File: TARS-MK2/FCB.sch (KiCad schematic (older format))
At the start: 30 parts, among them J101 505567-0681, J102 505567-0681, J103 505567-0681, J104 505567-0681, J105 505578-0671, J106 505578-0671, U101 LSM9DS1, U102 KX122-1711, U103 MS5611-01BA, U104 MPU-9250, U105 ublox_SAM-M8Q

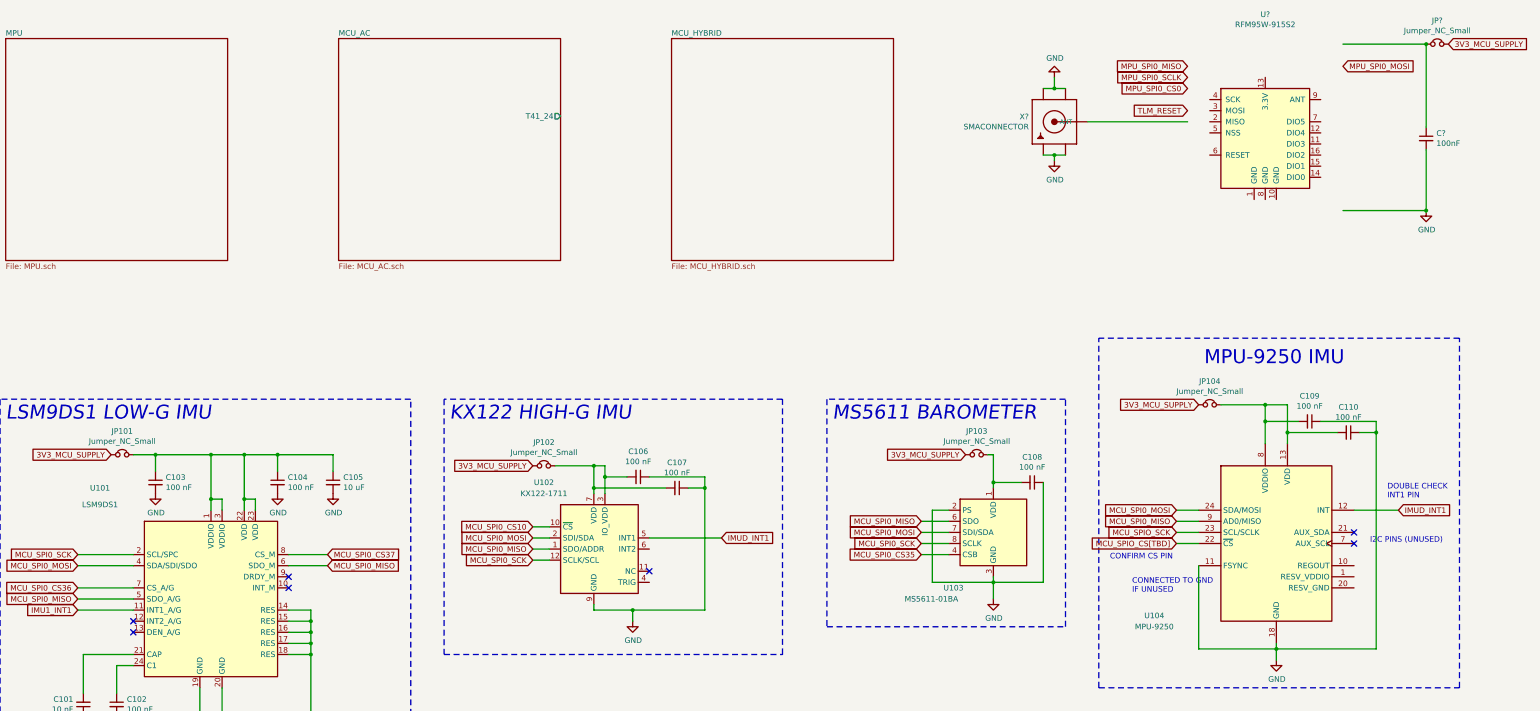
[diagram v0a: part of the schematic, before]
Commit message: Added MPU SYSBOOT config resistors
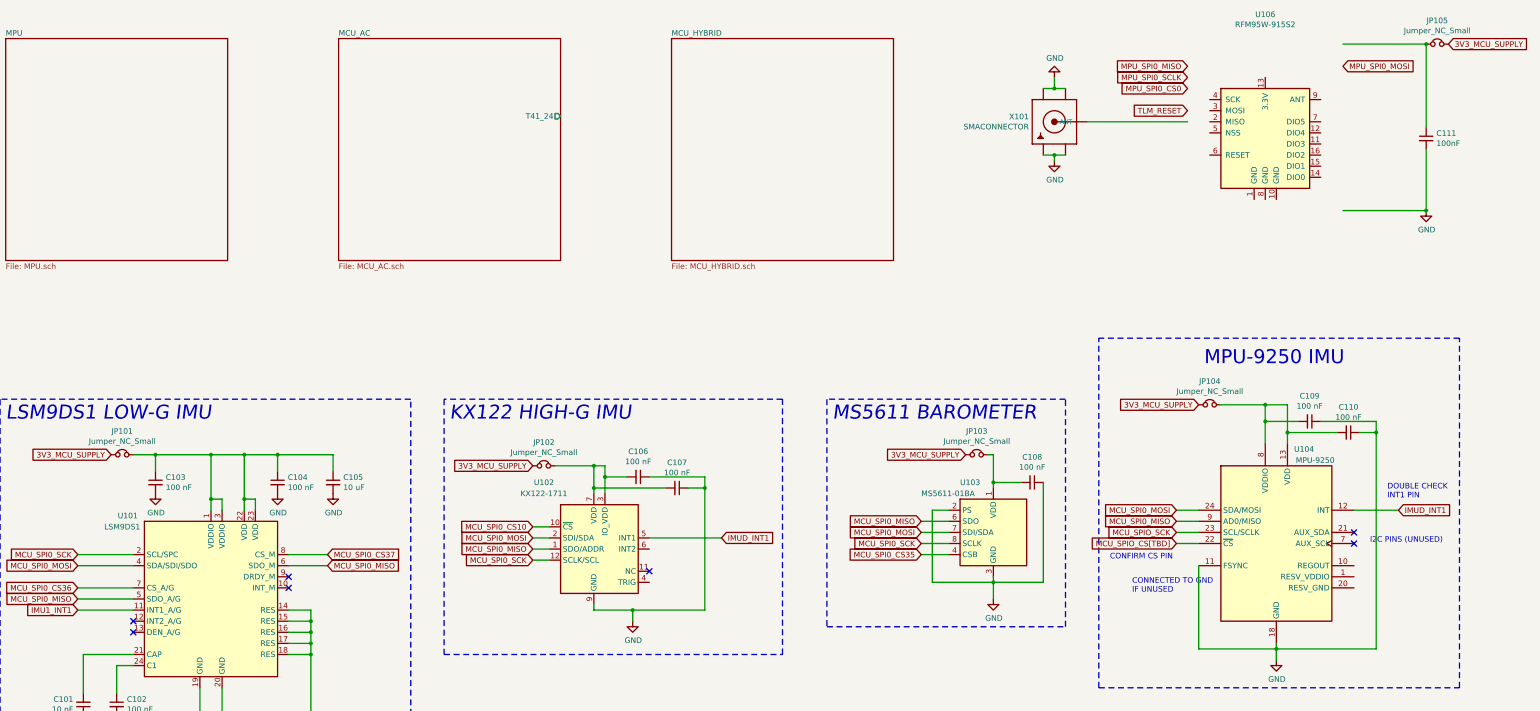
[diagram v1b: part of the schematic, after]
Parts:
- gave numbers to parts that had none: 4
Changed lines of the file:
@@
 F1 "MPU.sch" 50
-$EndSheet
-$Sheet
-S 7800 1500 2000 2000
-U 60021F93
-F0 "MCU_HYBRID" 50
-F1 "MCU_HYBRID.sch" 50
 $EndSheet
 Text Notes 11850 10500 0    67   Italic 0
@@
 U 1 1 602F3A3E
 P 10700 5950
-F 0 "U103" H 10250 5450 50  0000 L CNN
-F 1 "MS5611-01BA" H 9900 5350 50  0000 L CNN
+F 0 "U103" H 10400 6400 50  0000 L CNN
+F 1 "MS5611-01BA" H 10050 6300 50  0000 L CNN
 F 2 "Package_LGA:LGA-8_3x5mm_P1.25mm" H 10700 5950 50  0001 C CNN
 F 3 "https://www.te.com/commerce/DocumentDelivery/DDEController?Action=srchrtrv&DocNm=MS5611-01BA03&DocType=Data+Sheet&DocLang=English" H 10700 5950 50  0001 C CNN
@@
 Wire Wire Line
 	2450 6450 2950 6450
-Wire Wire Line
-	2450 6250 2950 6250
 Wire Wire Line
 	2450 6150 2950 6150
@@
 Text GLabel 2450 6450 0    50   Input ~ 0
 MCU_SPI0_CS36
-Text GLabel 2450 6250 0    50   Input ~ 0
-MCU_SPI0_MOSI
 Text GLabel 2450 6150 0    50   Input ~ 0
 MCU_SPI0_SCK
@@
 U 1 1 602BFCA3
 P 3650 6550
-F 0 "U101" H 2650 7550 50  0000 C CNN
-F 1 "LSM9DS1" H 2650 7400 50  0000 C CNN
+F 0 "U101" H 2900 7300 50  0000 C CNN
+F 1 "LSM9DS1" H 2850 7200 50  0000 C CNN
 F 2 "Package_LGA:LGA-24L_3x3.5mm_P0.43mm" H 5150 7300 50  0001 C CNN
 F 3 "http://www.st.com/content/ccc/resource/technical/document/datasheet/1e/3f/2a/d6/25/eb/48/46/DM00103319.pdf/files/DM00103319.pdf/jcr:content/translations/en.DM00103319.pdf" H 3650 6650 50  0001 C CNN
@@
 	0    -1   1    0
 $EndComp
-$Sheet
-S 4800 1500 2000 2000
-U 60021F5A
-F0 "MCU_AC" 50
-F1 "MCU_AC.sch" 50
-F2 "T41_24" O R 6800 2200 50
-$EndSheet
 Connection ~ 7100 5550
 Wire Wire Line
@@
 	13250 7100 13250 7000
 $Comp
-L power:GND #PWR?
+L power:GND #PWR0165
 U 1 1 606711D2
 P 13250 7100
-F 0 "#PWR?" H 13250 6850 50  0001 C CNN
+F 0 "#PWR0165" H 13250 6850 50  0001 C CNN
 F 1 "GND" H 13255 6927 50  0000 C CNN
 F 2 "" H 13250 7100 50  0001 C CNN
@@
 U 1 1 604AA87B
 P 13250 6050
-F 0 "U104" H 12150 5400 50  0000 C CNN
-F 1 "MPU-9250" H 12150 5300 50  0000 C CNN
+F 0 "U104" H 13500 6900 50  0000 C CNN
+F 1 "MPU-9250" H 13600 6800 50  0000 C CNN
 F 2 "Sensor_Motion:InvenSense_QFN-24_3x3mm_P0.4mm" H 13250 5050 50  0001 C CNN
 F 3 "https://store.invensense.com/datasheets/invensense/MPU9250REV1.0.pdf" H 13250 5900 50  0001 C CNN
@@
 MPU_SPI0_MOSI
 $Comp
-L RFM95W_915S2:RFM95W-915S2 U?
+L RFM95W_915S2:RFM95W-915S2 U106
 U 1 1 604CFE3B
 P 13150 2350
-F 0 "U?" H 13150 3417 50  0000 C CNN
+F 0 "U106" H 13150 3417 50  0000 C CNN
 F 1 "RFM95W-915S2" H 13150 3326 50  0000 C CNN
 F 2 "XCVR_RFM95W-915S2" H 13150 2350 50  0001 L BNN
@@
 	13850 1550 14600 1550
 $Comp
-L power:GND #PWR?
+L power:GND #PWR0166
 U 1 1 604E0CB3
 P 14600 3050
-F 0 "#PWR?" H 14600 2800 50  0001 C CNN
+F 0 "#PWR0166" H 14600 2800 50  0001 C CNN
 F 1 "GND" H 14605 2877 50  0000 C CNN
 F 2 "" H 14600 3050 50  0001 C CNN
@@
 $EndComp
 $Comp
-L D24V50F5:C_Small C?
+L D24V50F5:C_Small C111
 U 1 1 604E53FE
 P 14600 2400
-F 0 "C?" H 14692 2446 50  0000 L CNN
+F 0 "C111" H 14692 2446 50  0000 L CNN
 F 1 "100nF" H 14692 2355 50  0000 L CNN
 F 2 "" H 14600 2400 50  0001 C CNN
@@
 $EndComp
 $Comp
-L D24V50F5:Jumper_NC_Small JP?
+L D24V50F5:Jumper_NC_Small JP105
 U 1 1 604E6165
 P 14700 1550
-F 0 "JP?" H 14700 1762 50  0000 C CNN
+F 0 "JP105" H 14700 1762 50  0000 C CNN
 F 1 "Jumper_NC_Small" H 14700 1671 50  0000 C CNN
 F 2 "" H 14700 1550 50  0001 C CNN
@@
 $EndComp
 $Comp
-L SMACONNECTOR:SMACONNECTOR X?
+L SMACONNECTOR:SMACONNECTOR X101
 U 1 1 604E7810
 P 11250 2250
-F 0 "X?" H 11480 2204 50  0000 L CNN
+F 0 "X101" H 11480 2204 50  0000 L CNN
 F 1 "SMACONNECTOR" H 11480 2295 50  0000 L CNN
 F 2 "" H 11250 2250 50  0001 C CNN
@@
 	11150 2550 11250 2550
 $Comp
-L power:GND #PWR?
+L power:GND #PWR0167
 U 1 1 604F94E4
 P 11250 2600
-F 0 "#PWR?" H 11250 2350 50  0001 C CNN
+F 0 "#PWR0167" H 11250 2350 50  0001 C CNN
 F 1 "GND" H 11255 2427 50  0000 C CNN
 F 2 "" H 11250 2600 50  0001 C CNN
@@
 	11250 2550 11350 2550
 $Comp
-L power:GND #PWR?
+L power:GND #PWR0168
 U 1 1 604FE003
 P 11250 1850
-F 0 "#PWR?" H 11250 1600 50  0001 C CNN
+F 0 "#PWR0168" H 11250 1600 50  0001 C CNN
 F 1 "GND" H 11255 1677 50  0000 C CNN
 F 2 "" H 11250 1850 50  0001 C CNN
@@
 Wire Wire Line
 	12450 2250 11550 2250
+$Sheet
+S 7800 1500 2000 2000
+U 60021F93
+F0 "MCU_HYBRID" 50
+F1 "MCU_HYBRID.sch" 50
+$EndSheet
+Wire Wire Line
+	2450 6250 2950 6250
+Text GLabel 2450 6250 0    50   Input ~ 0
+MCU_SPI0_MOSI
+$Sheet
+S 4800 1500 2000 2000
+U 60021F5A
+F0 "MCU_AC" 50
+F1 "MCU_AC.sch" 50
+F2 "T41_24" O R 6800 2200 50
+$EndSheet
 $EndSCHEMATC

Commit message: Figured out trace/via tolerances
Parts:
- removed U106: RFM95W-915S2, XCVR_RFM95W-915S2, symbol RFM95W_915S2:RFM95W-915S2
- added DISP1: DISP_LCD_GENERIC_SPI_1.14IN_240X135_WRAPUNDER, 135x240_TFT_SCREEN:TFT_1.14IN_240X135_CUTOUT, symbol 240x135_TFT_SCREEN:DISP_LCD_GENERIC_SPI_1.14IN_240X135_WRAPUNDER
- added U106: RFM95W-915S2, RF_Module:HOPERF_RFM9XW_SMD, symbol RF_Module:RFM95W-915S2
- JP105: value Jumper_NC_Small -> TLM_JPR
- X101: value SMACONNECTOR -> SMA
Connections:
- net 3V3_MCU_SUPPLY is gone; now on net 3V3: JP101.1, JP102.1, JP103.1, JP104.1, JP105.2
- net MCU_SPI0_CS37 is gone; now on net LSM9_CS_AG: U101.8 (CS_M)
- net MCU_SPIO_SCK is gone; now on net SNS_SPI_MISO: U104.23 (SCL/SCLK)
- net GND: now also J105.1, J105.6, J106.1, J106.6, U106.1 (GND), U106.10 (GND), U106.8 (GND)
- net GND1: now also J101.P1 (SHIELD), J101.P2 (SHIELD), J102.P1 (SHIELD), J102.P2 (SHIELD), J103.P1 (SHIELD), J103.P2 (SHIELD), J104.P1 (SHIELD), J104.P2 (SHIELD), J105.P1, J105.P2, J106.P1, J106.P2
- net MPU_SPI0_MISO: now also U106.2 (MISO)
- net MPU_SPI0_MOSI: now also U106.3 (MOSI)
- net LSM9_INT_M: now reaches U101.10 (INT_M)
- net LSM9_INT2_AG: now reaches U101.12 (INT2_A/G)
- net LSM9_DRDY_M: now reaches U101.9 (DRDY_M)
- net KX122_INT2: now reaches U102.6 (INT2)
- net 3V3: now reaches J105.2
- net 3V3: now also J105.5, J106.2, J106.5
- net 5V: now reaches J105.3
- net 5V: now also J105.4, J106.3, J106.4
- net at C111.1, JP105.1: now also U106.13 (3.3V)
- net at X101.ANTENNA (ANT): now also U106.9 (ANT)
- net IMU1_INT1 renamed LSM9_INT1_AG
- net IMUD_INT1 renamed KX122_INT1
- net KX122_INT1: no longer U104.12 (INT)
- net MCU_SPI0_CS10 renamed KX122_CS
- net MCU_SPI0_CS35 renamed MS5611_CS
- net MCU_SPI0_CS36 renamed LSM9_CS_AG
- net MCU_SPI0_MISO renamed SNS_SPI_MISO
- net SNS_SPI_MISO: no longer U104.9 (AD0/MISO)
- net MCU_SPI0_MOSI renamed SNS_SPI_MOSI
- net SNS_SPI_MOSI: now also U104.9 (AD0/MISO); no longer U104.24 (SDA/MOSI)
- net MCU_SPI0_SCK renamed SNS_SPI_SCK
- net SNS_SPI_SCK: now also U104.24 (SDA/MOSI)
- net MCU_SPIO_CS[TBD] renamed TLM_CS
- net TLM_CS: now also U106.5 (NSS)
- new net: DISP1.13 (GND), DISP1.8 (GND)
- new net MPU9250_INT: U104.12 (INT)
- new net MPU_SPI0_SCK: U106.4 (SCK)
- new net TLM_DIO0: U106.14 (DIO0)
- new net TLM_DIO1: U106.15 (DIO1)
- new net TLM_DIO2: U106.16 (DIO2)
- new net TLM_DIO3: U106.11 (DIO3)
- new net TLM_DIO4: U106.12 (DIO4)
- new net TLM_DIO5: U106.7 (DIO5)
- new net TLM_RST: U106.6 (RESET)
- no-connect marks 7 -> 4
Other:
- note added: "<----------- the fuck?"
- note added: "BOARD-TO-BOARD CONN."
- note added: "LoRa TELEMETRY"
- note added: "the fuck? ----------->"
- note removed: "DOUBLE CHECK \nINT1 PIN"
- moved on the sheet: C101, C102, C103, C104, C105, C106, C107, C108, C109, C110, C111, J101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

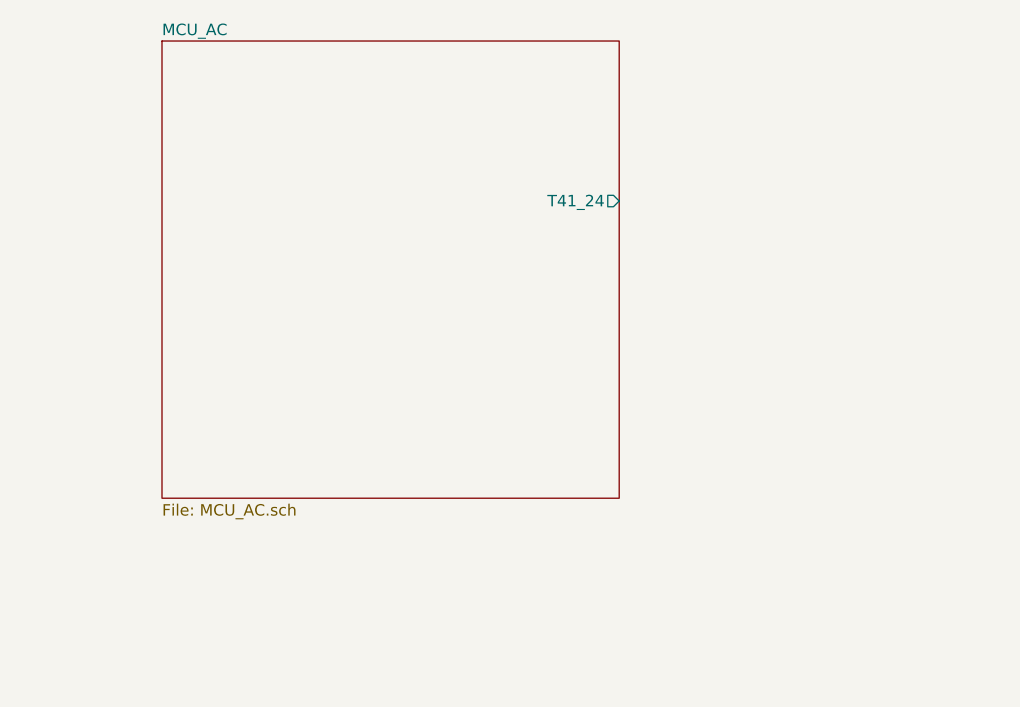
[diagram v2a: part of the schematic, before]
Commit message: Wired sensors to MCU
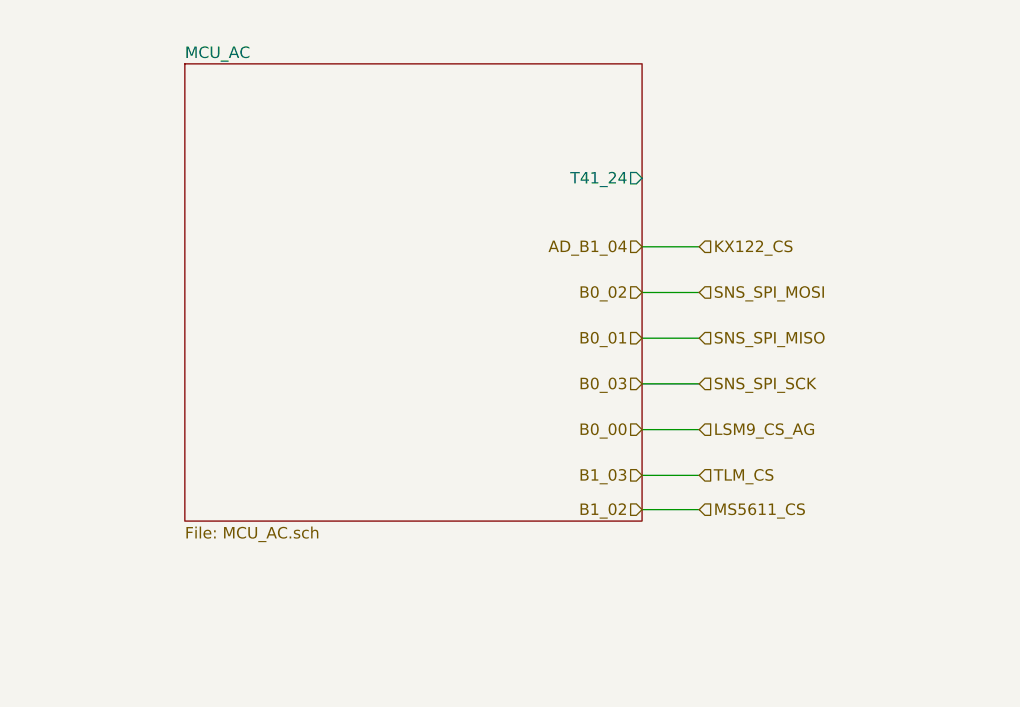
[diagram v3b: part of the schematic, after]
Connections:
- net KX122_CS renamed AD_B1_04
- net LSM9_CS_AG renamed B0_00
- net MS5611_CS renamed B1_02
- net SNS_SPI_MISO renamed B0_01
- net SNS_SPI_MOSI renamed B0_02
- net SNS_SPI_SCK renamed B0_03
- net TLM_CS renamed B1_03
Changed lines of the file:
@@
 $EndSheet
 $Sheet
-S 7150 1450 2000 2000
+S 7250 1550 2000 2000
 U 60021F5A
 F0 "MCU_AC" 50
 F1 "MCU_AC.sch" 50
-F2 "T41_24" O R 9150 2150 50
+F2 "T41_24" O R 9250 2050 50
 $EndSheet
 $Comp
@@
 Text HLabel 6000 9900 2    50   Output ~ 0
 KX122_INT2
+Text HLabel 9250 2550 0    50   Input ~ 0
+B0_02
+Text HLabel 9500 2550 2    50   Input ~ 0
+SNS_SPI_MOSI
+Wire Wire Line
+	9250 2550 9500 2550
+Text HLabel 9250 2750 0    50   Input ~ 0
+B0_01
+Text HLabel 9500 2750 2    50   Input ~ 0
+SNS_SPI_MISO
+Wire Wire Line
+	9250 2750 9500 2750
+Text HLabel 9250 2950 0    50   Input ~ 0
+B0_03
+Text HLabel 9500 2950 2    50   Input ~ 0
+SNS_SPI_SCK
+Wire Wire Line
+	9250 2950 9500 2950
+Text HLabel 9250 3150 0    50   Input ~ 0
+B0_00
+Text HLabel 9500 3150 2    50   Input ~ 0
+LSM9_CS_AG
+Wire Wire Line
+	9250 3150 9500 3150
+Text HLabel 9250 3350 0    50   Input ~ 0
+B1_03
+Text HLabel 9500 3350 2    50   Input ~ 0
+TLM_CS
+Wire Wire Line
+	9250 3350 9500 3350
+Text HLabel 9250 3500 0    50   Input ~ 0
+B1_02
+Text HLabel 9500 3500 2    50   Input ~ 0
+MS5611_CS
+Wire Wire Line
+	9250 3500 9500 3500
+Text HLabel 9250 2350 0    50   Input ~ 0
+AD_B1_04
+Text HLabel 9500 2350 2    50   Input ~ 0
+KX122_CS
+Wire Wire Line
+	9250 2350 9500 2350
 $EndSCHEMATC
